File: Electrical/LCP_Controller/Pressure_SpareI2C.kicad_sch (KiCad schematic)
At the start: 4 parts, among them J8 SALEAE_TEST, Q9 TSM500P02CX RFG

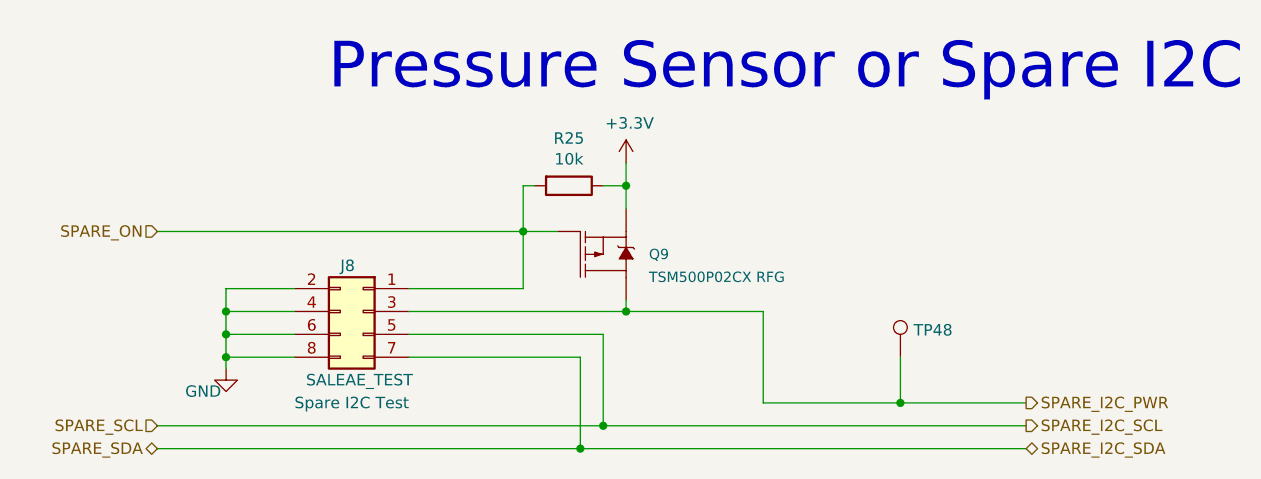
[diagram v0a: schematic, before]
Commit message: Hardware Revision : v0.3
1. modified schematic design, removed unnecessary test points.
2. pcb layout 2x8 Inches allowance dimension, layout is in progress
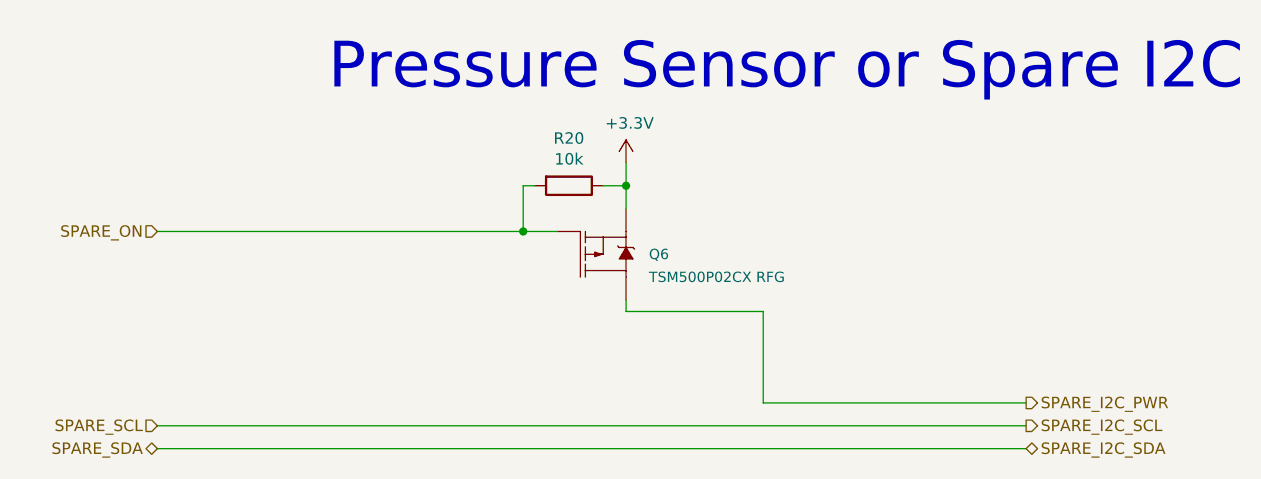
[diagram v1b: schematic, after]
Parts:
- removed J8: SALEAE_TEST, Connector_PinHeader_2.54mm:PinHeader_2x04_P2.54mm_Vertical, symbol Connector_Generic:Conn_02x04_Odd_Even
- removed TP48: 5004, TestPoint:TestPoint_Keystone_5000-5004_Miniature, symbol Connector:TestPoint
- renumbered Q9 to Q6, R25 to R20
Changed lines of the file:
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@@
     (comment 5 "Current design modified by: Basharat Martin")
-  )
-  (junction (at 140.97 93.98) (diameter 0) (color 0 0 0 0)
-  )
-  (junction (at 96.52 93.98) (diameter 0) (color 0 0 0 0)
-  )
-  (junction (at 171.45 104.14) (diameter 0) (color 0 0 0 0)
-  )
-  (junction (at 138.43 106.68) (diameter 0) (color 0 0 0 0)
   )
   (junction (at 140.97 80.01) (diameter 0) (color 0 0 0 0)
   )
-  (junction (at 135.89 109.22) (diameter 0) (color 0 0 0 0)
-  )
-  (junction (at 96.52 99.06) (diameter 0) (color 0 0 0 0)
-  )
   (junction (at 129.54 85.09) (diameter 0) (color 0 0 0 0)
-  )
-  (junction (at 96.52 96.52) (diameter 0) (color 0 0 0 0)
   )
   (wire (pts (xy 129.54 85.09) (xy 129.54 80.01))
     (stroke (width 0) (type default) (color 0 0 0 0))
   )
-  (wire (pts (xy 96.52 93.98) (xy 96.52 96.52))
-    (stroke (width 0) (type default) (color 0 0 0 0))
-  )
-  (wire (pts (xy 88.9 106.68) (xy 138.43 106.68))
-    (stroke (width 0) (type default) (color 0 0 0 0))
-  )
   (wire (pts (xy 129.54 80.01) (xy 130.81 80.01))
-    (stroke (width 0) (type default) (color 0 0 0 0))
-  )
-  (wire (pts (xy 135.89 99.06) (xy 135.89 109.22))
     (stroke (width 0) (type default) (color 0 0 0 0))
   )
@@
     (stroke (width 0) (type default) (color 0 0 0 0))
   )
-  (wire (pts (xy 138.43 106.68) (xy 185.42 106.68))
-    (stroke (width 0) (type default) (color 0 0 0 0))
-  )
-  (wire (pts (xy 185.42 104.14) (xy 171.45 104.14))
+  (wire (pts (xy 88.9 106.68) (xy 185.42 106.68))
     (stroke (width 0) (type default) (color 0 0 0 0))
   )
@@
     (stroke (width 0) (type default) (color 0 0 0 0))
   )
-  (wire (pts (xy 104.14 99.06) (xy 96.52 99.06))
+  (wire (pts (xy 156.21 104.14) (xy 185.42 104.14))
     (stroke (width 0) (type default) (color 0 0 0 0))
   )
-  (wire (pts (xy 96.52 93.98) (xy 96.52 91.44))
-    (stroke (width 0) (type default) (color 0 0 0 0))
-  )
-  (wire (pts (xy 135.89 109.22) (xy 185.42 109.22))
-    (stroke (width 0) (type default) (color 0 0 0 0))
-  )
-  (wire (pts (xy 171.45 104.14) (xy 156.21 104.14))
-    (stroke (width 0) (type default) (color 0 0 0 0))
-  )
-  (wire (pts (xy 116.84 99.06) (xy 135.89 99.06))
-    (stroke (width 0) (type default) (color 0 0 0 0))
-  )
-  (wire (pts (xy 116.84 93.98) (xy 140.97 93.98))
-    (stroke (width 0) (type default) (color 0 0 0 0))
-  )
-  (wire (pts (xy 96.52 96.52) (xy 96.52 99.06))
-    (stroke (width 0) (type default) (color 0 0 0 0))
-  )
-  (wire (pts (xy 104.14 93.98) (xy 96.52 93.98))
-    (stroke (width 0) (type default) (color 0 0 0 0))
-  )
-  (wire (pts (xy 88.9 109.22) (xy 135.89 109.22))
-    (stroke (width 0) (type default) (color 0 0 0 0))
-  )
-  (wire (pts (xy 138.43 96.52) (xy 138.43 106.68))
-    (stroke (width 0) (type default) (color 0 0 0 0))
-  )
-  (wire (pts (xy 171.45 99.06) (xy 171.45 104.14))
+  (wire (pts (xy 88.9 109.22) (xy 185.42 109.22))
     (stroke (width 0) (type default) (color 0 0 0 0))
   )
@@
     (stroke (width 0) (type default) (color 0 0 0 0))
   )
-  (wire (pts (xy 104.14 96.52) (xy 96.52 96.52))
-    (stroke (width 0) (type default) (color 0 0 0 0))
-  )
-  (wire (pts (xy 96.52 91.44) (xy 104.14 91.44))
-    (stroke (width 0) (type default) (color 0 0 0 0))
-  )
-  (wire (pts (xy 96.52 99.06) (xy 96.52 100.33))
-    (stroke (width 0) (type default) (color 0 0 0 0))
-  )
-  (wire (pts (xy 116.84 96.52) (xy 138.43 96.52))
-    (stroke (width 0) (type default) (color 0 0 0 0))
-  )
   (wire (pts (xy 138.43 80.01) (xy 140.97 80.01))
     (stroke (width 0) (type default) (color 0 0 0 0))
   )
   (wire (pts (xy 140.97 93.98) (xy 140.97 92.71))
-    (stroke (width 0) (type default) (color 0 0 0 0))
-  )
-  (wire (pts (xy 116.84 91.44) (xy 129.54 91.44))
-    (stroke (width 0) (type default) (color 0 0 0 0))
-  )
-  (wire (pts (xy 129.54 91.44) (xy 129.54 85.09))
     (stroke (width 0) (type default) (color 0 0 0 0))
   )
@@
   (symbol (lib_id "SparkFun-DiscreteSemi:MOSFET_PCH-DMG2307L") (at 138.43 87.63 0) (mirror x) (unit 1)
     (in_bom yes) (on_board yes)
-    (property "Reference" "Q9" (id 0) (at 143.51 87.63 0)
+    (property "Reference" "Q6" (id 0) (at 143.51 87.63 0)
       (effects (font (size 1.143 1.143)) (justify left))
     )
@@
   (symbol (lib_id "power:+3.3V") (at 140.97 77.47 0) (unit 1)
     (in_bom yes) (on_board yes)
-    (property "Reference" "#PWR067" (id 0) (at 140.97 81.28 0)
+    (property "Reference" "#PWR060" (id 0) (at 140.97 81.28 0)
       (effects (font (size 1.27 1.27)) hide)
     )
@@
   (symbol (lib_id "Device:R") (at 134.62 80.01 270) (unit 1)
     (in_bom yes) (on_board yes)
-    (property "Reference" "R25" (id 0) (at 134.62 74.7522 90))
+    (property "Reference" "R20" (id 0) (at 134.62 74.7522 90))
     (property "Value" "10k" (id 1) (at 134.62 77.0636 90))
     (property "Footprint" "Resistor_SMD:R_0805_2012Metric" (id 2) (at 134.62 78.232 90)
@@
     (pin "2")
   )
-  (symbol (lib_id "Connector:TestPoint") (at 171.45 99.06 0) (unit 1)
-    (in_bom yes) (on_board yes)
-    (property "Reference" "TP48" (id 0) (at 172.9232 96.0628 0)
-      (effects (font (size 1.27 1.27)) (justify left))
-    )
-    (property "Value" "5004" (id 1) (at 172.9232 98.3742 0)
-      (effects (font (size 1.27 1.27)) (justify left) hide)
-    )
-    (property "Footprint" "TestPoint:TestPoint_Keystone_5000-5004_Miniature" (id 2) (at 176.53 99.06 0)
-      (effects (font (size 1.27 1.27)) hide)
-    )
-    (property "Datasheet" "~" (id 3) (at 176.53 99.06 0)
-      (effects (font (size 1.27 1.27)) hide)
-    )
-    (property "TestPoint" "Spare_I2C_PWR" (id 4) (at 171.45 99.06 0)
-      (effects (font (size 1.27 1.27)) hide)
-    )
-    (property "MPN" "" (id 5) (at 171.45 99.06 0)
-      (effects (font (size 1.27 1.27)) hide)
-    )
-    (pin "1")
-  )
-  (symbol (lib_id "Connector_Generic:Conn_02x04_Odd_Even") (at 111.76 93.98 0) (mirror y) (unit 1)
-    (in_bom yes) (on_board yes)
-    (property "Reference" "J8" (id 0) (at 109.22 88.9 0)
-      (effects (font (size 1.27 1.27)) (justify right))
-    )
-    (property "Value" "SALEAE_TEST" (id 1) (at 105.41 101.6 0)
-      (effects (font (size 1.27 1.27)) (justify right))
-    )
-    (property "Footprint" "Connector_PinHeader_2.54mm:PinHeader_2x04_P2.54mm_Vertical" (id 2) (at 111.76 93.98 0)
-      (effects (font (size 1.27 1.27)) hide)
-    )
-    (property "Datasheet" "~" (id 3) (at 111.76 93.98 0)
-      (effects (font (size 1.27 1.27)) hide)
-    )
-    (property "TestPoint" "Spare I2C Test" (id 4) (at 110.49 104.14 0))
-    (property "MPN" "0010897080" (id 5) (at 111.76 93.98 0)
-      (effects (font (size 1.27 1.27)) hide)
-    )
-    (pin "1")
-    (pin "2")
-    (pin "3")
-    (pin "4")
-    (pin "5")
-    (pin "6")
-    (pin "7")
-    (pin "8")
-  )
-  (symbol (lib_id "power:GND") (at 96.52 100.33 0) (unit 1)
-    (in_bom yes) (on_board yes)
-    (property "Reference" "#PWR064" (id 0) (at 96.52 106.68 0)
-      (effects (font (size 1.27 1.27)) hide)
-    )
-    (property "Value" "GND" (id 1) (at 93.98 102.87 0))
-    (property "Footprint" "" (id 2) (at 96.52 100.33 0)
-      (effects (font (size 1.27 1.27)) hide)
-    )
-    (property "Datasheet" "" (id 3) (at 96.52 100.33 0)
-      (effects (font (size 1.27 1.27)) hide)
-    )
-    (pin "1")
-  )
 )
